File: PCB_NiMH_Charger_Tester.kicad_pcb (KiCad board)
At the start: 2 copper layers, 94.9 x 77.5 mm, 63 parts, among them J1 USB_C_Receptacle_PowerOnly_6P, J2 USB_C_Receptacle_USB2.0_16P, J3 UPDI v2 header, J4 SSD1306, J5 Serial Header, Q1 DTC114EL, Q2 DTA114EL, Q3 MTB060P06I3, Q4 MTA100N10KRI3, SW1 SW_Push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

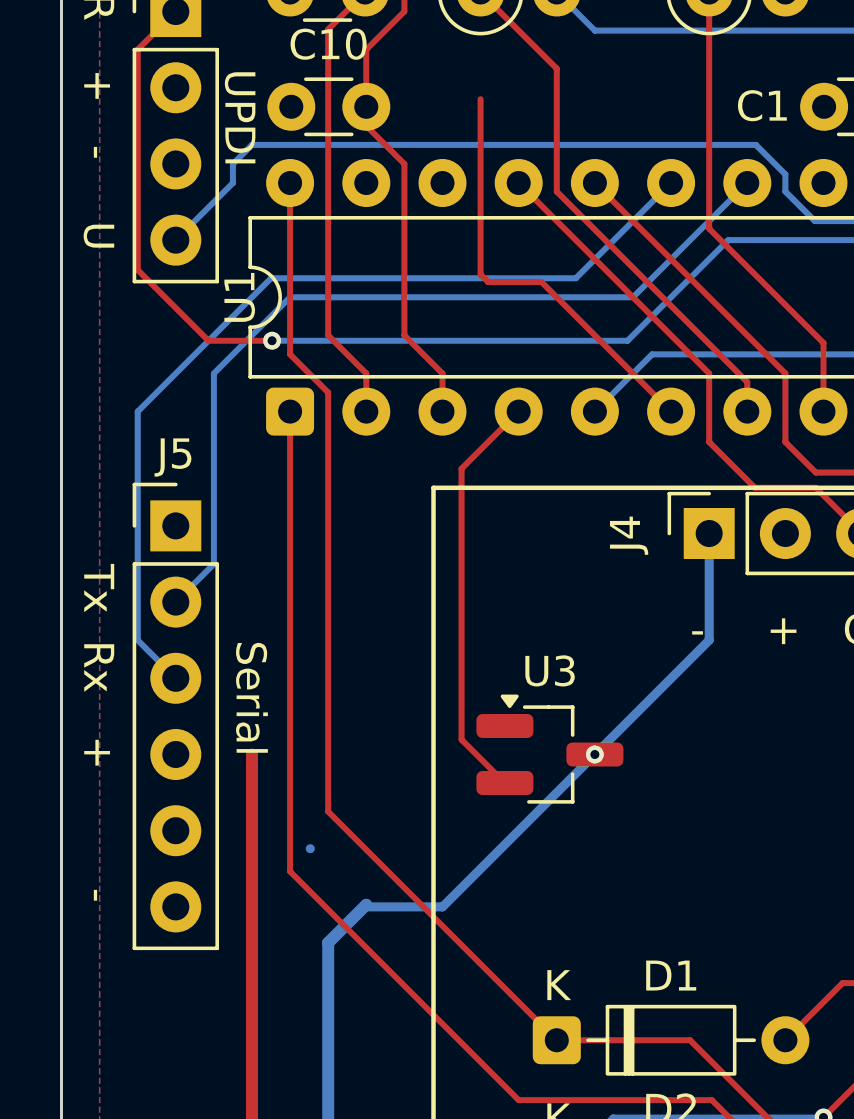
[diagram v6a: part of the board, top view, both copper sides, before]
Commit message: Reverse Serial Header
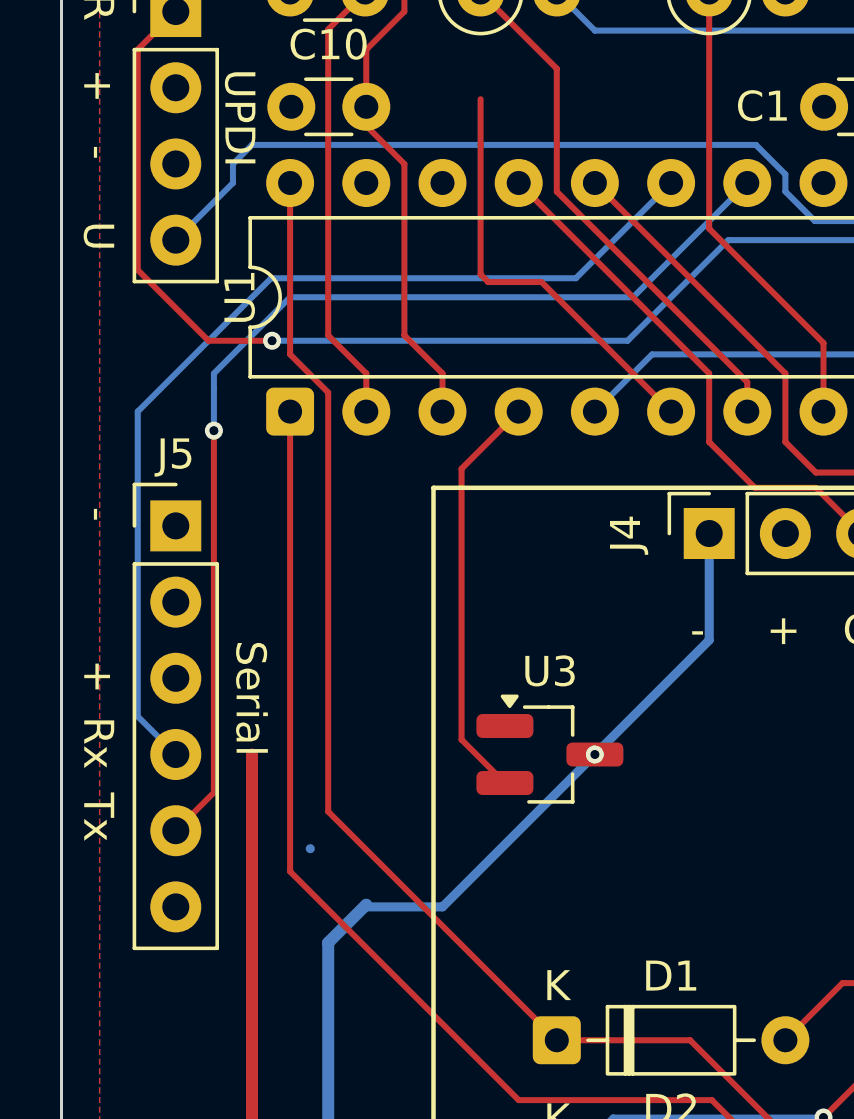
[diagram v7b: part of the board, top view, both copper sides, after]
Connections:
- J5 pad 1: unconnected-(J5-Pin_1-Pad1) -> GND
- J5 pad 2: TX -> unconnected-(J5-Pin_2-Pad2)
- J5 pad 3: RX -> +5V
- J5 pad 4: +5V -> RX
- J5 pad 5: unconnected-(J5-Pin_5-Pad5) -> TX
- J5 pad 6: GND -> unconnected-(J5-Pin_6-Pad6)
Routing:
- net TX: track 28.6 -> 36.2 mm, vias 0 -> 1
- net RX: track 30.4 -> 32.9 mm
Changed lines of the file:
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@@
 	(title_block
 		(title "NiMH Charger & Tester")
-		(date "2025-08-25")
+		(date "2025-09-05")
 		(rev "2")
 		(company "K.Takata")
@@
 	(net 53 "unconnected-(J2-SBU2-PadB8)")
 	(net 54 "unconnected-(J2-SBU1-PadA8)")
-	(net 55 "unconnected-(J5-Pin_1-Pad1)")
-	(net 56 "unconnected-(J5-Pin_5-Pad5)")
+	(net 55 "unconnected-(J5-Pin_6-Pad6)")
+	(net 56 "unconnected-(J5-Pin_2-Pad2)")
 	(footprint "Button_Switch_THT:SW_PUSH_6mm"
 		(layer "F.Cu")
@@
 			(layers "*.Cu" "*.Mask")
 			(remove_unused_layers no)
-			(net 55 "unconnected-(J5-Pin_1-Pad1)")
+			(net 2 "GND")
 			(pinfunction "Pin_1")
-			(pintype "passive+no_connect")
+			(pintype "passive")
 		)
 		(pad "2" thru_hole circle
@@
 			(layers "*.Cu" "*.Mask")
 			(remove_unused_layers no)
-			(net 26 "TX")
+			(net 56 "unconnected-(J5-Pin_2-Pad2)")
 			(pinfunction "Pin_2")
-			(pintype "passive")
+			(pintype "passive+no_connect")
 		)
 		(pad "3" thru_hole circle
@@
 			(layers "*.Cu" "*.Mask")
 			(remove_unused_layers no)
-			(net 27 "RX")
+			(net 4 "+5V")
 			(pinfunction "Pin_3")
 			(pintype "passive")
@@
 			(layers "*.Cu" "*.Mask")
 			(remove_unused_layers no)
-			(net 4 "+5V")
+			(net 27 "RX")
 			(pinfunction "Pin_4")
 			(pintype "passive")
@@
 			(layers "*.Cu" "*.Mask")
 			(remove_unused_layers no)
-			(net 56 "unconnected-(J5-Pin_5-Pad5)")
+			(net 26 "TX")
 			(pinfunction "Pin_5")
-			(pintype "passive+no_connect")
+			(pintype "passive")
 		)
 		(pad "6" thru_hole circle
@@
 			(layers "*.Cu" "*.Mask")
 			(remove_unused_layers no)
-			(net 2 "GND")
+			(net 55 "unconnected-(J5-Pin_6-Pad6)")
 			(pinfunction "Pin_6")
-			(pintype "passive")
+			(pintype "passive+no_connect")
 		)
 		(embedded_fonts no)
@@
 	)
 	(gr_text "Rx"
-		(at 50.165 68.58 270)
+		(at 50.165 71.12 270)
 		(layer "F.SilkS")
 		(effects
@@
 	)
 	(gr_text "+"
-		(at 50.165 71.755 270)
+		(at 50.165 69.215 270)
 		(layer "F.SilkS")
 		(effects
@@
 	)
 	(gr_text "Tx"
-		(at 50.165 66.04 270)
+		(at 50.165 73.66 270)
 		(layer "F.SilkS")
 		(effects
@@
 	)
 	(gr_text "-"
-		(at 50.165 76.835 270)
+		(at 50.165 64.135 270)
 		(layer "F.SilkS")
 		(effects
@@
 	)
 	(segment
+		(start 54.61 73.66)
+		(end 53.34 74.93)
+		(width 0.2)
+		(layer "F.Cu")
+		(net 26)
+	)
+	(segment
+		(start 54.61 61.595)
+		(end 54.61 73.66)
+		(width 0.2)
+		(layer "F.Cu")
+		(net 26)
+	)
+	(via
+		(at 54.61 61.595)
+		(size 0.6)
+		(drill 0.3)
+		(layers "F.Cu" "B.Cu")
+		(net 26)
+	)
+	(segment
 		(start 68.58 57.15)
 		(end 72.39 53.34)
@@
 	)
 	(segment
-		(start 53.34 67.31)
-		(end 54.61 66.04)
+		(start 54.61 59.69)
+		(end 54.61 60.198)
 		(width 0.2)
 		(layer "B.Cu")
@@
 	)
 	(segment
-		(start 54.61 66.04)
-		(end 54.61 59.69)
+		(start 54.61 59.69)
+		(end 57.15 57.15)
 		(width 0.2)
 		(layer "B.Cu")
@@
 	)
 	(segment
-		(start 54.61 59.69)
-		(end 57.15 57.15)
+		(start 54.61 60.198)
+		(end 54.61 61.595)
 		(width 0.2)
 		(layer "B.Cu")
@@
 	)
 	(segment
-		(start 66.675 56.515)
-		(end 69.85 53.34)
+		(start 52.07 60.96)
+		(end 52.07 71.12)
 		(width 0.2)
 		(layer "B.Cu")
@@
 	(segment
 		(start 56.515 56.515)
-		(end 66.675 56.515)
+		(end 52.07 60.96)
 		(width 0.2)
 		(layer "B.Cu")
@@
 	)
 	(segment
-		(start 53.34 69.85)
-		(end 52.07 68.58)
+		(start 66.675 56.515)
+		(end 56.515 56.515)
 		(width 0.2)
 		(layer "B.Cu")
@@
 	)
 	(segment
-		(start 52.07 68.58)
-		(end 52.07 60.96)
+		(start 69.85 53.34)
+		(end 66.675 56.515)
 		(width 0.2)
 		(layer "B.Cu")
@@
 	)
 	(segment
-		(start 52.07 60.96)
-		(end 56.515 56.515)
+		(start 52.07 71.12)
+		(end 53.34 72.39)
 		(width 0.2)
 		(layer "B.Cu")
